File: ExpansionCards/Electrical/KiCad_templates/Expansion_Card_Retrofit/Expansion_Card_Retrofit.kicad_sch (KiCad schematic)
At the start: 30 parts, among them J1 HDMI_A, P2 USB_C_Plug, U1 MS2130, U2 GD25D05CT, U3 USBLC6-2P6, Y1 Crystal

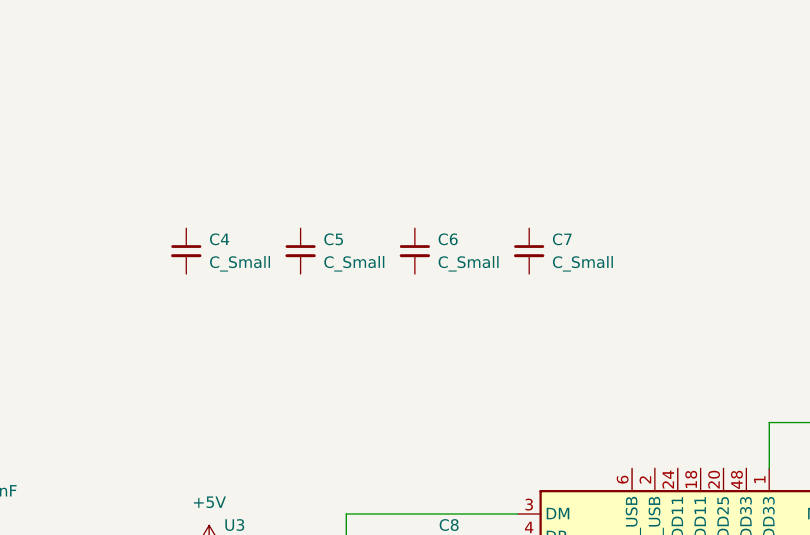
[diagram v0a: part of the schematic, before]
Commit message: Change PCB to 4 Layer and improve routing
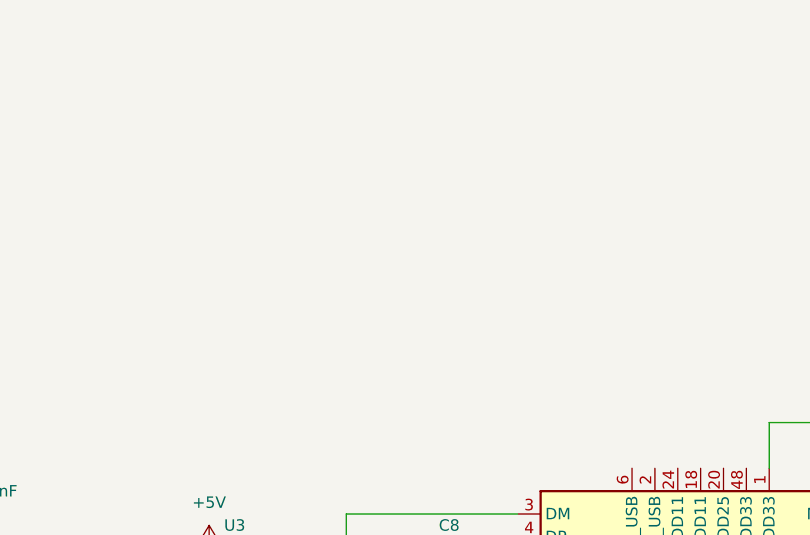
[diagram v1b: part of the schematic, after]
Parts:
- removed C4, C5, C6, C7: C_Small, Capacitor_SMD:C_0201_0603Metric, symbol Device:C_Small
- J1: footprint Connector_Video:HDMI_A_Molex_208658-1001_Horizontal -> Connector_Video:HDMI_A_Amphenol_10029449-x01xLF_Horizontal

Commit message: Finished PCB design and add gerber files and BOM
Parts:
- added C4, C5, C6, C7: C22uF, Capacitor_SMD:C_0201_0603Metric, symbol Device:C
- added L1, L2, L3, L4: L2.2uH, Inductor_SMD:L_0201_0603Metric, symbol Device:L
- added R10: R100K, Resistor_SMD:R_0201_0603Metric_Pad0.64x0.40mm_HandSolder, symbol Device:R
- added R11: R680K, Resistor_SMD:R_0201_0603Metric, symbol Device:R
- added R12: R470K, Resistor_SMD:R_0201_0603Metric, symbol Device:R
- added R13, R14: R100K, Resistor_SMD:R_0201_0603Metric, symbol Device:R
- added R15, R16, R17: R150K, Resistor_SMD:R_0201_0603Metric, symbol Device:R
- added R18: R180K, Resistor_SMD:R_0201_0603Metric, symbol Device:R
- added U4: ~, Package_DFN_QFN:HVQFN-24-1EP_4x4mm_P0.5mm_EP2.1x2.1mm, symbol EA3059_lib:EA3059
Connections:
- net +5V: now also R10.2, U4.11 (VIN1), U4.20 (VIN4), U4.23 (VIN3), U4.3 (VCC), U4.8 (VIN2)
- net GND: now also C4.2, C5.2, C6.2, C7.2, R14.1, R15.1, R16.1, R18.1, U4.1 (GND3), U4.13 (GND1), U4.18 (GND4), U4.4 (AGND), U4.6 (GND2)
- net +3.3V: now reaches U1.1 (DVDD33), U1.16 (DVDD33), U1.31 (DVDD33), U1.33 (DVDD33), U1.41 (DVDD33), U2.3 (~{WP}), U2.8 (VCC)
- net +3.3V: now also U1.2 (AVDD33_USB), U1.48 (AVDD33), U1.5 (AVDD33_USB), U1.52 (AVDD33), U1.56 (AVDD33), U1.60 (AVDD33), U1.8 (AVDD33_USB), C4.1, L1.1, R11.2
- net +1V1: now reaches U1.10 (AVDD11_USB), U1.12 (AVDD11_USB), U1.6 (AVDD11_USB)
- net +1V1: now also U1.18 (DVDD11), U1.24 (AVDD11), U1.39 (DVDD11), U1.51 (AVDD11), U1.55 (AVDD11), U1.59 (AVDD11), C7.1, L4.1, R17.2
- net +2V5: now reaches U1.20 (AVDD25), U1.23 (AVDD25), U1.47 (AVDD25)
- net +2V5: now also C5.1, L2.1, R12.2
- new net: R13.1, R14.2, U4.2 (FB3)
- new net: R11.1, R15.2, U4.14 (FB1)
- new net: L1.2, U4.12 (LX1)
- new net: L3.2, U4.24 (LX3)
- new net: R17.1, R18.2, U4.17 (FB4)
- new net: R12.1, R16.2, U4.5 (FB2)
- new net: R10.1, U4.10 (EN1), U4.21 (EN4), U4.22 (EN3), U4.9 (EN2)
- new net: L4.2, U4.19 (LX4)
- new net: L2.2, U4.7 (LX2)
- new net +1V2: C6.1, L3.1, R13.2
